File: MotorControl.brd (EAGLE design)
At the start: 69 x 57 mm, 47 parts, among them IC1 ESP32-WROOM-32E8M, IC2 TB6612FNG, U3 TP4056, U4 SPX3940AM3-L-3-3/TR, U5 INTERFACE-FT230XS-R(SSOP16)

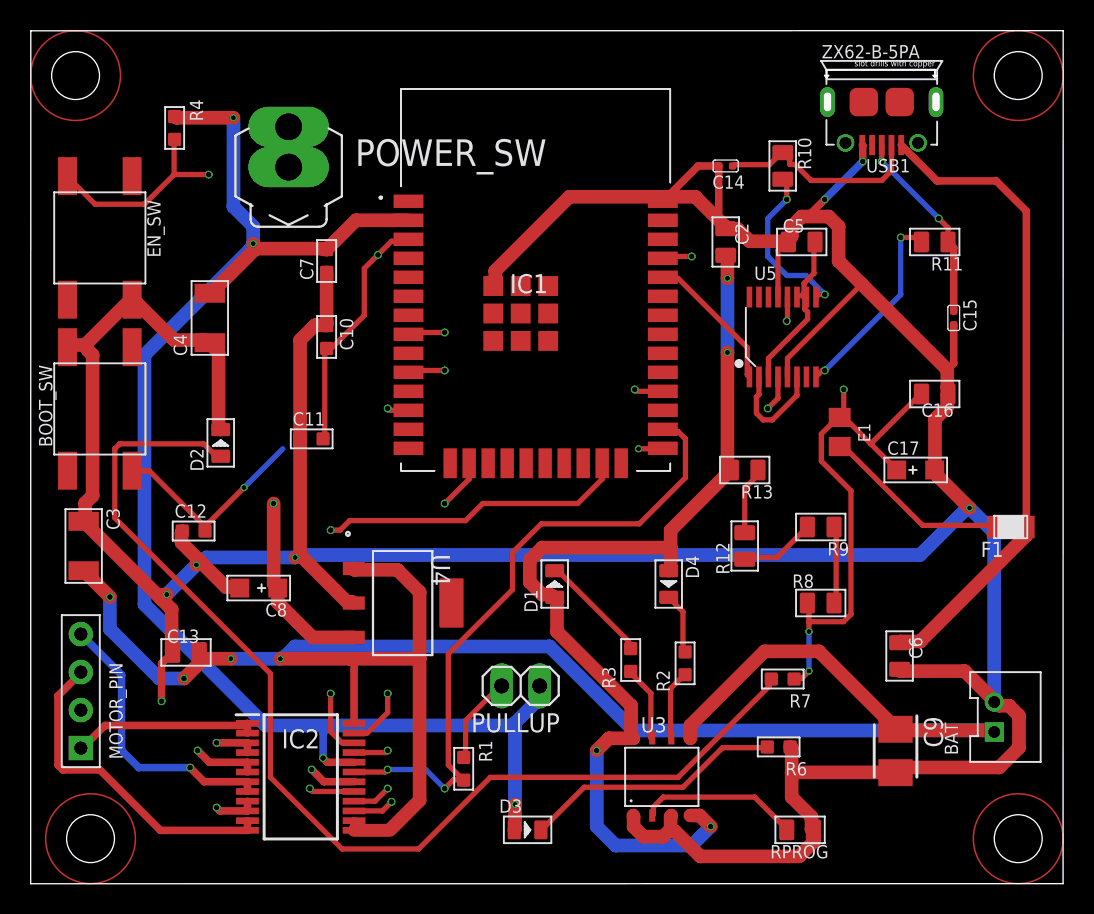
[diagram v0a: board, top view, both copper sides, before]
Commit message: [Fix] ボード図においてGNDをbottomに配線
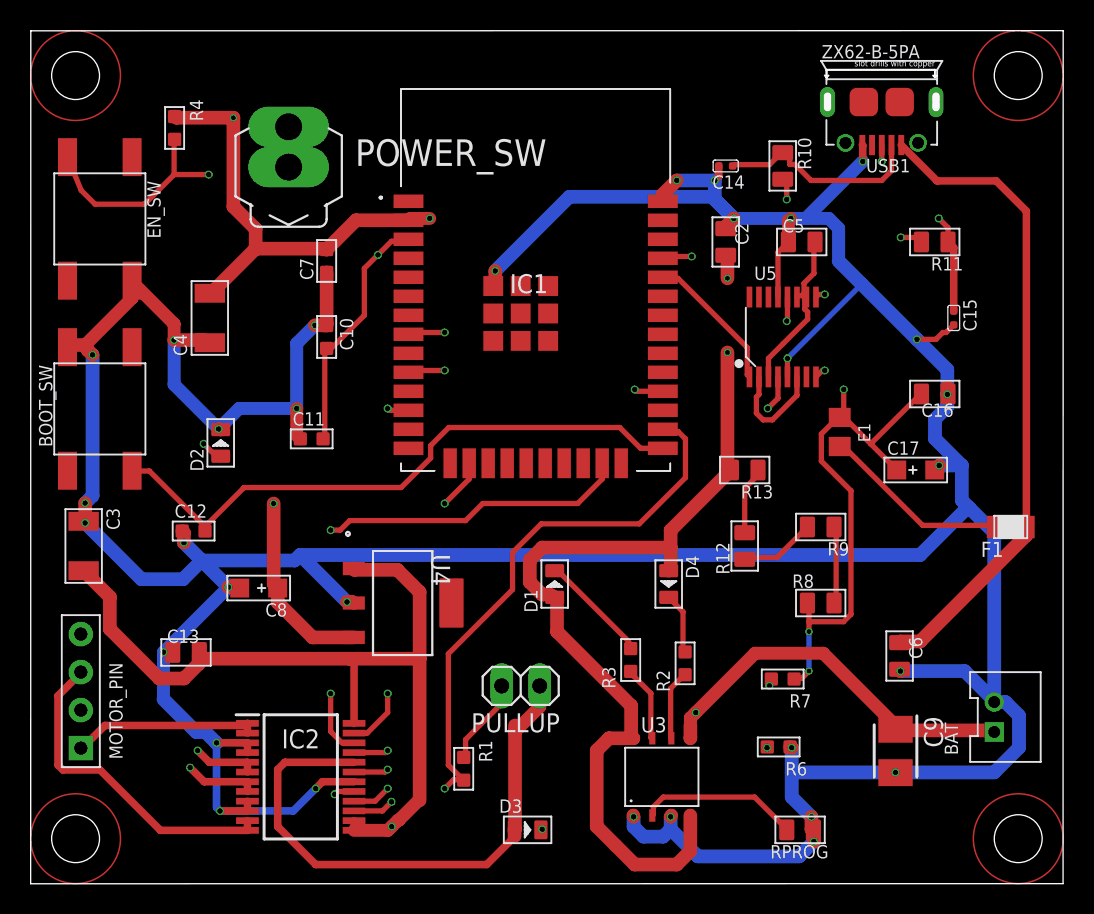
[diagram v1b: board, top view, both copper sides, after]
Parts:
- moved EN_SW 1.27 mm to (4.62, 44.4)
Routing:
- net B+: track 133.3 -> 107.3 mm, vias 4 -> 2
- net N$30: track 16.0 -> 41.4 mm, vias 2 -> 0
- net BIN1: track 32.7 -> 37.5 mm
- net +3V3: track 102.7 -> 106.4 mm, vias 4 -> 2
- net N$3: track 74.3 -> 75.8 mm, vias 0 -> 2
- net N$29: track 43.8 -> 44.8 mm
- net GND: track 309.6 -> 310.3 mm, vias 10 -> 31
- net VIN+: track 66.2 -> 65.9 mm, vias 4 -> 2
- net N$14: vias 0 -> 2
